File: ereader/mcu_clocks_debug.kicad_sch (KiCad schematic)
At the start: 21 parts, among them J1 Cortex Debug 10-pin, U1 R7KA8P1KFLCAC#UC0, U2 TPS389001DSET, Y1 24MHz, Y2 32.768kHz

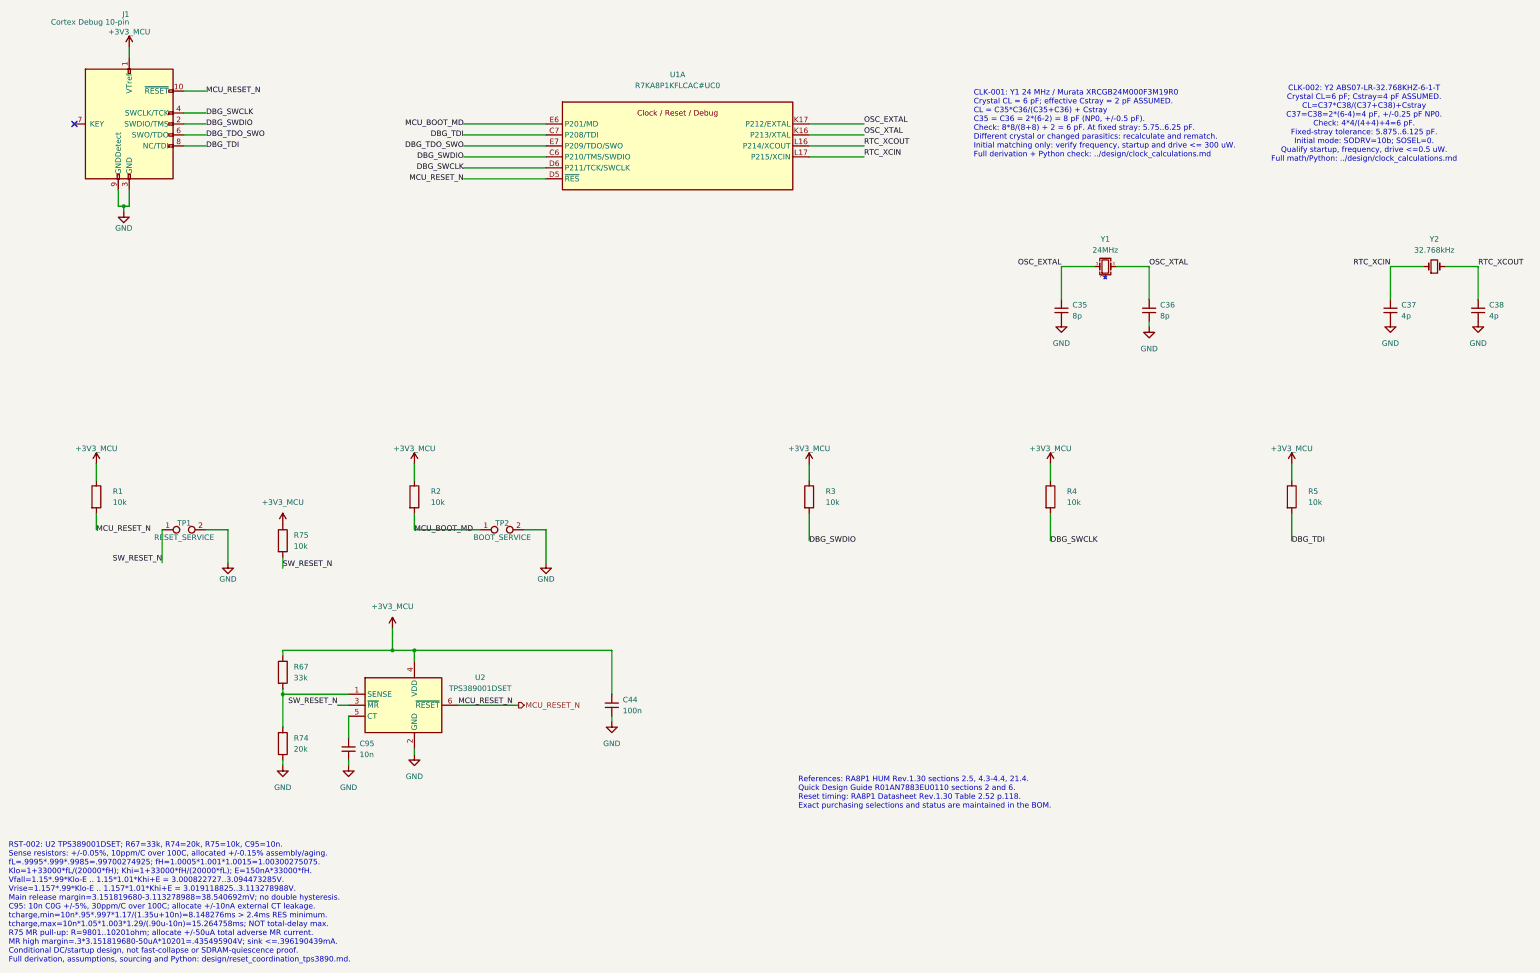
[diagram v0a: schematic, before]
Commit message: WIP: integrate orientation sensor and refresh schematic review exports
Add LIS2DW12 host wiring and sourced passives, revise held-supply discharge calculations, document camera and capacitance screens, and refresh standard capacitor caches. Include reviewed 14-page PDF and reconciled native BOM. ERC remains 111 errors and 11 warnings; electrical design is incomplete. Refs #21.
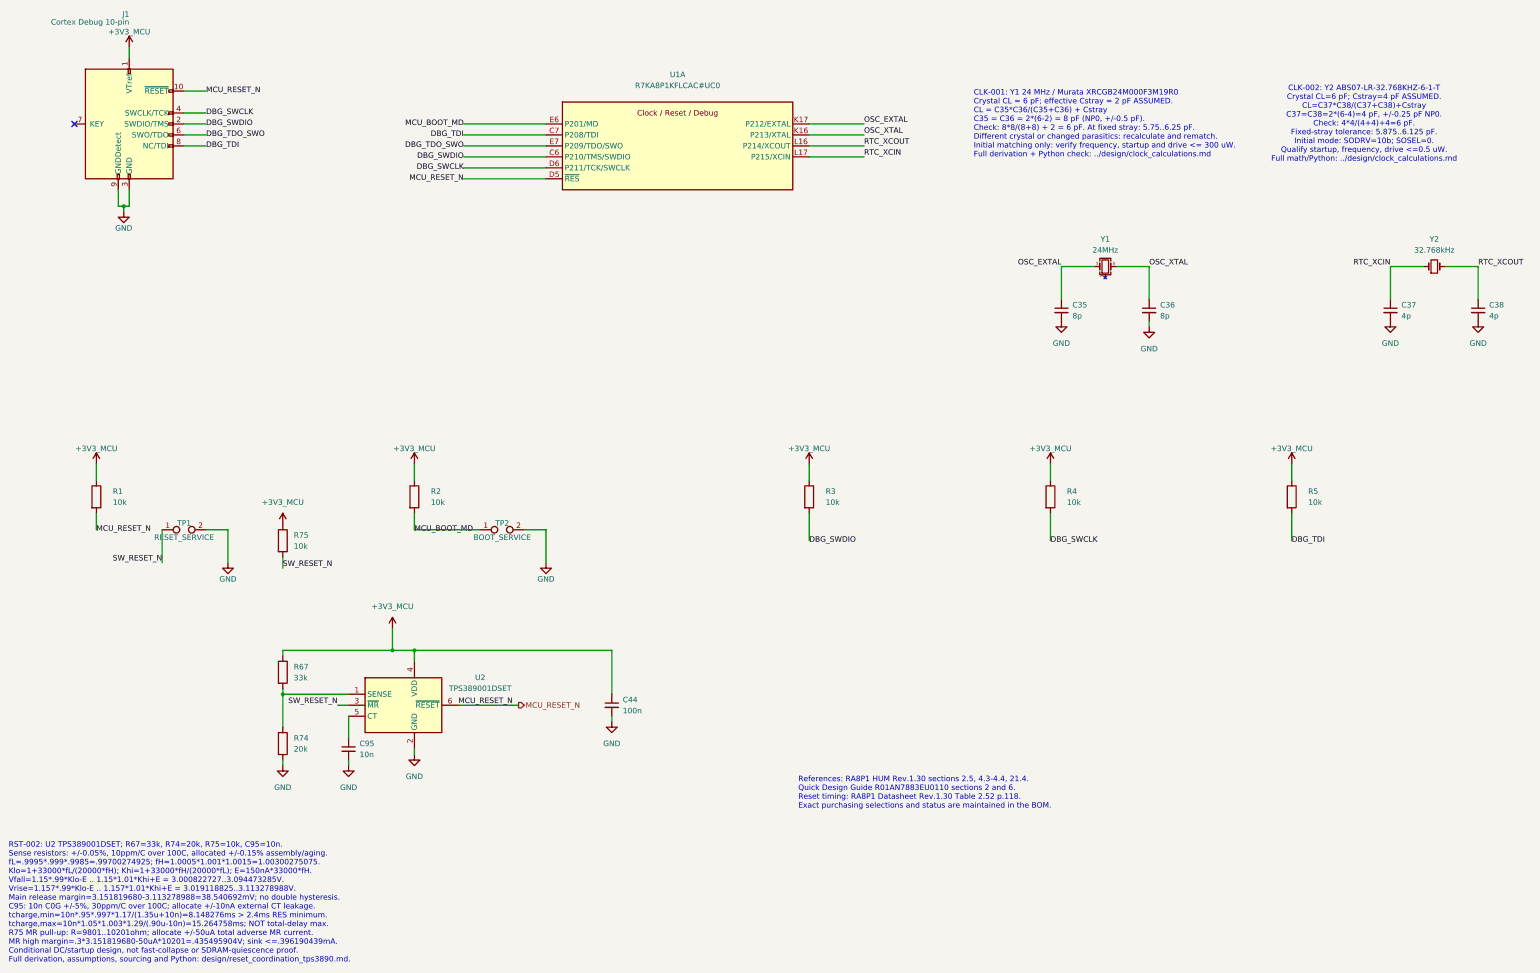
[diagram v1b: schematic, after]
